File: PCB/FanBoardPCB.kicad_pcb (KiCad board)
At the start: 2 copper layers, 41.8 x 29.5 mm, 29 parts, among them J1 FanBrdConn, J2 FAN1, J3 FAN1, J4 FAN1, J6 FAN1, Q1 IRLML0030, Q2 IRLML0030, Q3 IRLML0030, Q5 IRLML0030

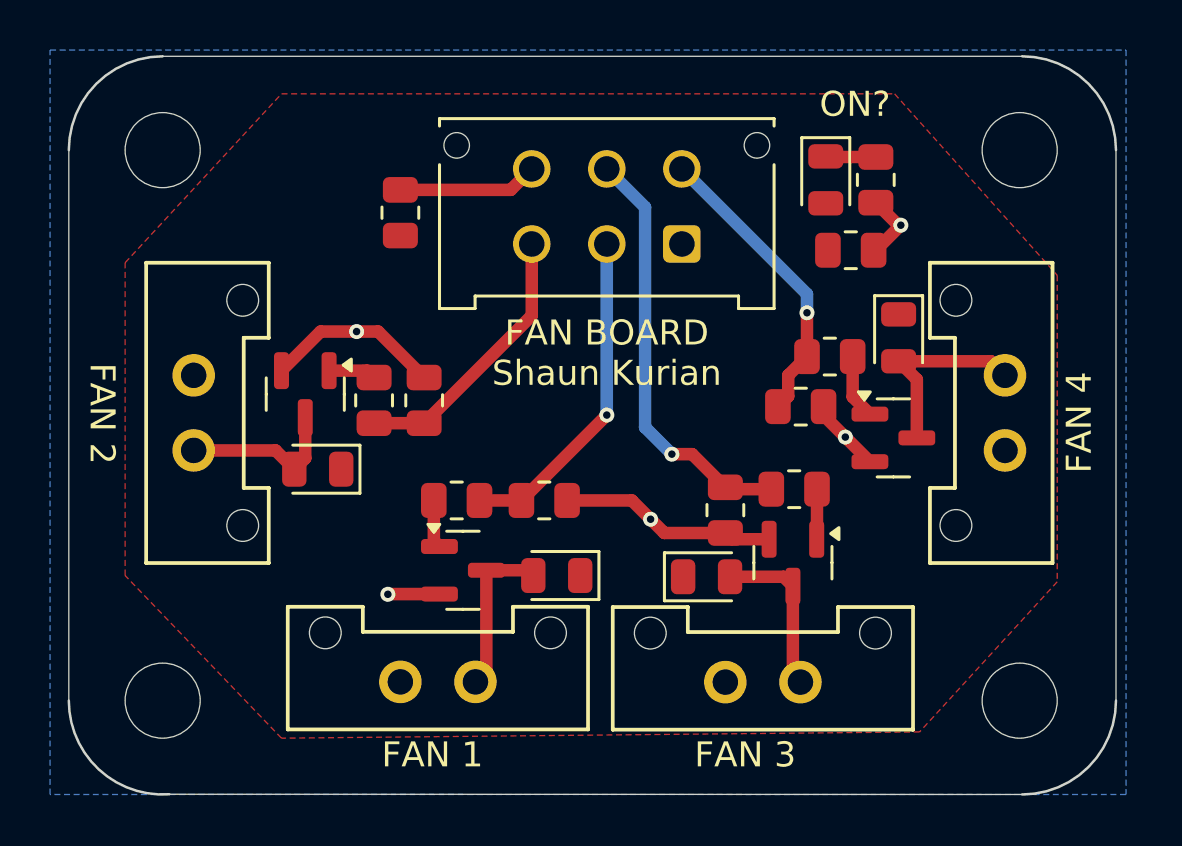
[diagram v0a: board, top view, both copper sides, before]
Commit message: Modified PCB layout to reduce trace/via amounts.
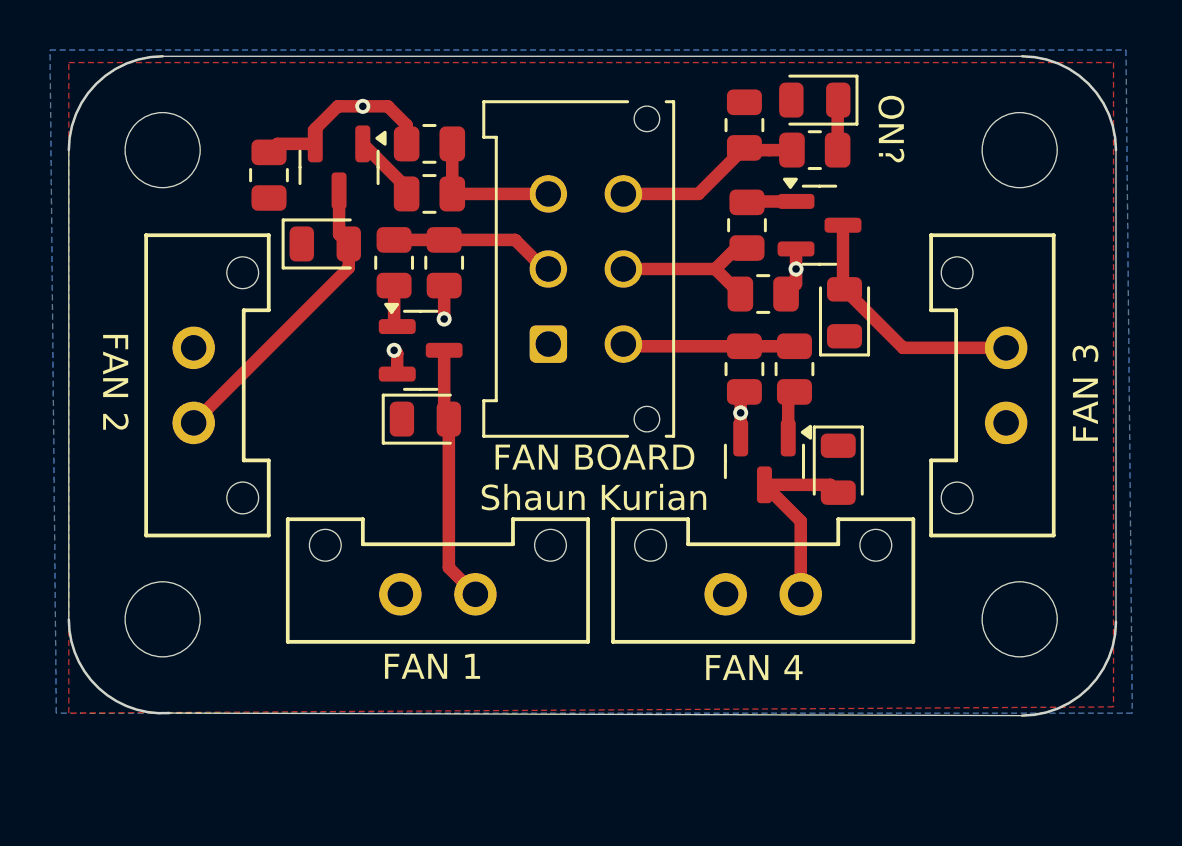
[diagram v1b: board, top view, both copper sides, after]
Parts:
- moved J3 15.3 mm to (166.0, 57.1), turned to 90 degrees
- moved Q2 13.5 mm to (158.5, 49.2), turned to 0 degrees
- moved J4 12.6 mm to (154.8, 64.0), turned to 0 degrees
- moved D2 11.9 mm to (159.5, 52.8), turned to 90 degrees
- moved R7 10.7 mm to (155.6, 49.2), turned to 90 degrees
- moved R2 10.3 mm to (143.5, 50.8), turned to -90 degrees
- moved R4 10.3 mm to (142.9, 46.0), turned to 180 degrees
- moved R3 9.82 mm to (141.5, 50.8), turned to -90 degrees
- moved Q1 9.16 mm to (139.3, 46.9)
- moved D1 9.00 mm to (138.8, 50.0), turned to 0 degrees
- moved Q5 8.95 mm to (142.6, 54.2)
- moved R6 8.77 mm to (156.2, 52.0), turned to 0 degrees
- moved R5 8.54 mm to (142.9, 48.0), turned to 180 degrees
- moved D5 8.16 mm to (142.8, 57.0), turned to 0 degrees
- moved J1 6.67 mm to (147.7, 54.0), turned to 90 degrees
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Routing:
- net /FAN3: track 17.0 -> 6.70 mm, vias 1 -> 0
- net GND: track 29.5 -> 21.4 mm
- net /FAN1: track 13.3 -> 6.64 mm, vias 1 -> 0
- net Net-(D1-A): track 6.58 -> 12.0 mm
- net /FAN4: track 12.1 -> 6.87 mm, vias 1 -> 0
- net /FAN2: track 10.9 -> 5.84 mm
- net Net-(D5-A): track 6.60 -> 10.3 mm
- net Net-(D2-A): track 6.63 -> 10.0 mm
- net Net-(Q1-G): track 1.91 -> 2.72 mm
- net Net-(Q3-G): track 2.59 -> 1.94 mm
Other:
- board size 41.8 x 29.5 mm -> 41.8 x 26.3 mm

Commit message: Updated footprints/layout for better connections.
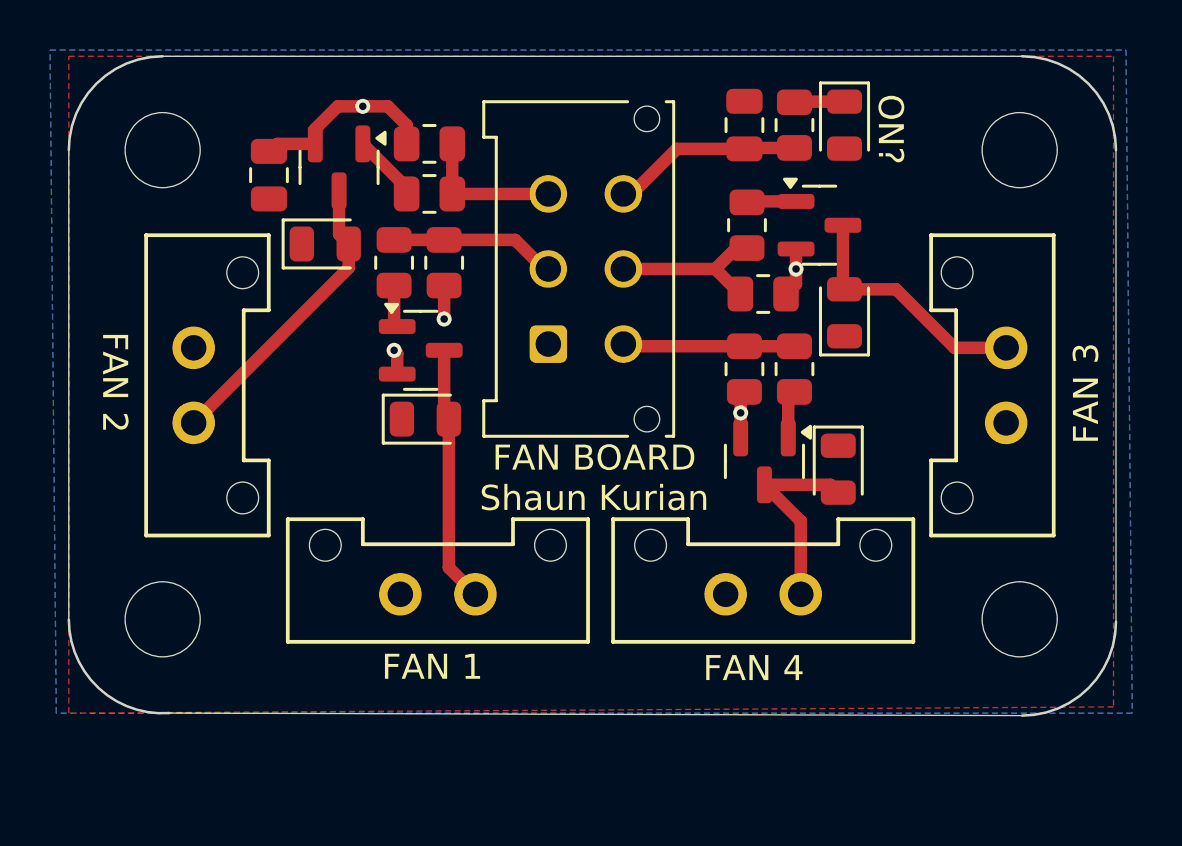
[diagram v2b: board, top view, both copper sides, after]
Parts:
- C1, C2: footprint Resistor_SMD:R_0805_2012Metric -> Capacitor_SMD:C_0805_2012Metric
- D1, D2, D3, D5: footprint LED_SMD:LED_0805_2012Metric -> Diode_SMD:D_0805_2012Metric
- moved STATUS_LED1 1.55 mm to (159.5, 45.2), turned to -90 degrees
- moved R1 1.29 mm to (157.5, 45.2), turned to -90 degrees

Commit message: Layout #3 for PCB.
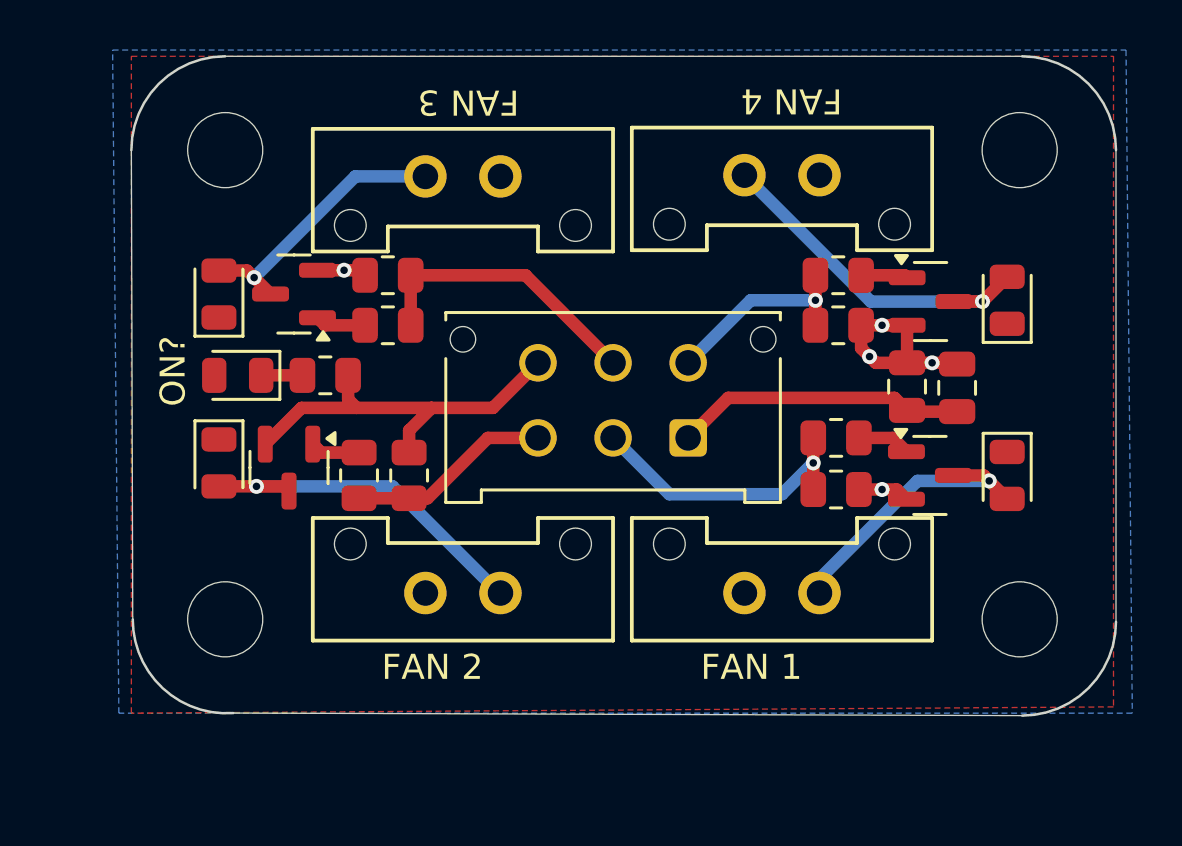
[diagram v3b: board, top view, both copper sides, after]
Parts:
- moved C1 26.9 mm to (162.0, 55.7)
- moved STATUS_LED1 26.2 mm to (135.2, 55.2), turned to 180 degrees
- moved D2 25.0 mm to (134.5, 52.0)
- moved D5 23.4 mm to (166.0, 59.2), turned to -90 degrees
- moved J3 22.5 mm to (145.8, 47.3), turned to 180 degrees
- moved R1 21.2 mm to (138.8, 55.2), turned to 0 degrees
- moved Q2 21.2 mm to (137.5, 52.0), turned to 180 degrees
- moved Q5 21.0 mm to (162.9, 59.2)
- moved R3 19.0 mm to (159.2, 57.8), turned to 0 degrees
- moved R2 18.1 mm to (159.2, 59.8), turned to 0 degrees
- moved J4 17.2 mm to (158.5, 47.2), turned to 180 degrees
- moved R6 15.0 mm to (141.2, 51.2), turned to 180 degrees
- moved R7 14.9 mm to (141.2, 53.2), turned to 180 degrees
- moved J6 13.8 mm to (155.5, 64.0)
- moved C2 13.5 mm to (164.0, 55.8), turned to 90 degrees
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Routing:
- net +12V: track 0.00 -> 11.8 mm
- net GND: track 21.5 -> 28.7 mm
- net Net-(D3-A): track 8.06 -> 14.1 mm, vias 0 -> 1
- net /FAN1: track 6.64 -> 11.5 mm, vias 0 -> 1
- net /FAN3: track 6.70 -> 11.5 mm
- net Net-(D1-A): track 12.0 -> 14.4 mm, vias 0 -> 1
- net /FAN2: track 5.84 -> 8.15 mm
- net /FAN4: track 6.87 -> 8.12 mm, vias 0 -> 1
- net Net-(D5-A): track 10.3 -> 11.5 mm, vias 0 -> 1
- net Net-(D2-A): track 10.0 -> 11.0 mm, vias 0 -> 1
- net Net-(Q1-G): track 2.72 -> 1.99 mm
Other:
- board size 41.8 x 26.3 mm -> 39.3 x 26.3 mm

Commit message: Flipped the MOLEX for clip to face inward.
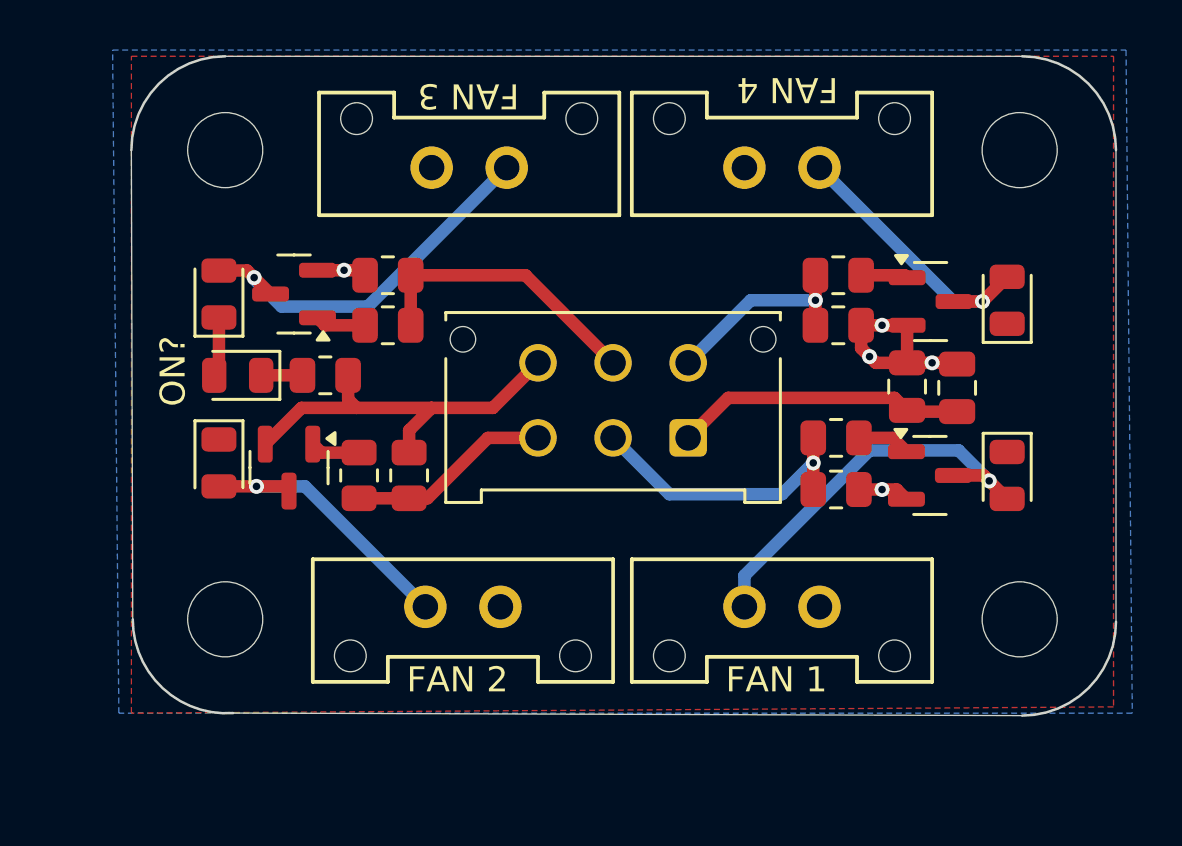
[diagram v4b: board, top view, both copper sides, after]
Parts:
- moved J2 3.05 mm to (145.8, 64.5), turned to 180 degrees
- moved J6 3.05 mm to (158.5, 64.5), turned to 180 degrees
- moved J4 3.01 mm to (155.5, 47.0), turned to 0 degrees
- moved J3 2.77 mm to (143.0, 47.0), turned to 0 degrees
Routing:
- net Net-(D5-A): track 11.5 -> 16.1 mm
- net Net-(D2-A): track 11.0 -> 15.4 mm
- net Net-(D3-A): track 14.1 -> 11.3 mm
- net Net-(D1-A): track 14.4 -> 11.6 mm
- net +12V: track 11.8 -> 14.2 mm
